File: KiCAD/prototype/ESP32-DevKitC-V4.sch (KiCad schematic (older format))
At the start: 27 parts

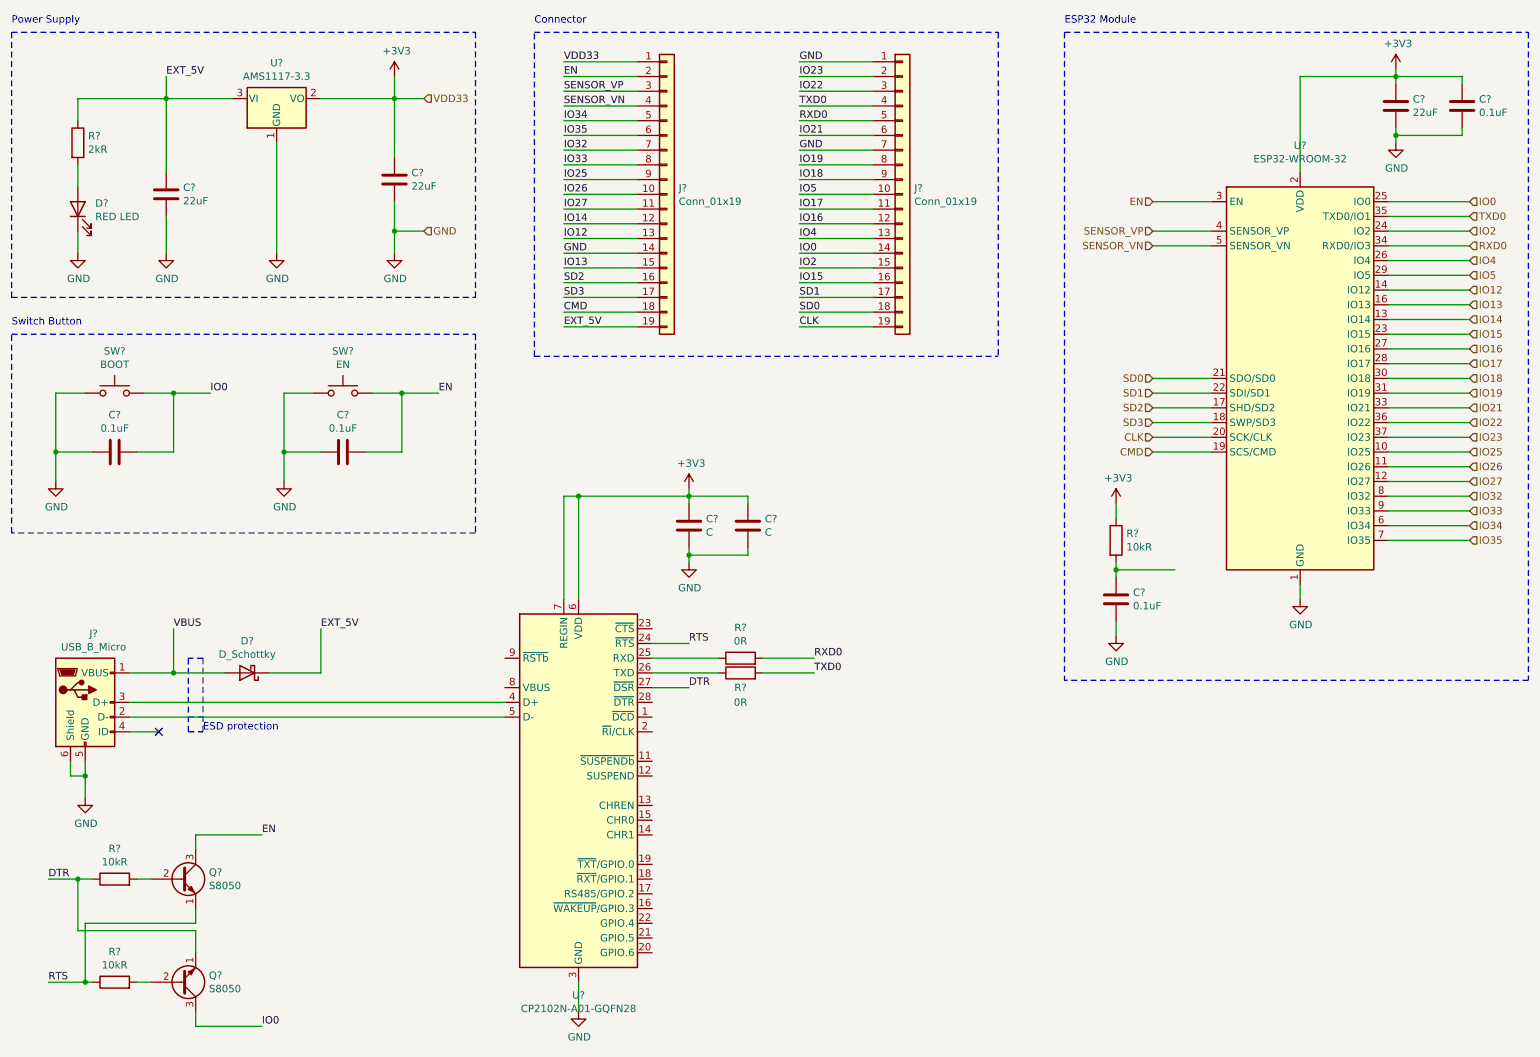
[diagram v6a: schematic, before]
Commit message: Add missing connections on ESP32-DevKitC-V4
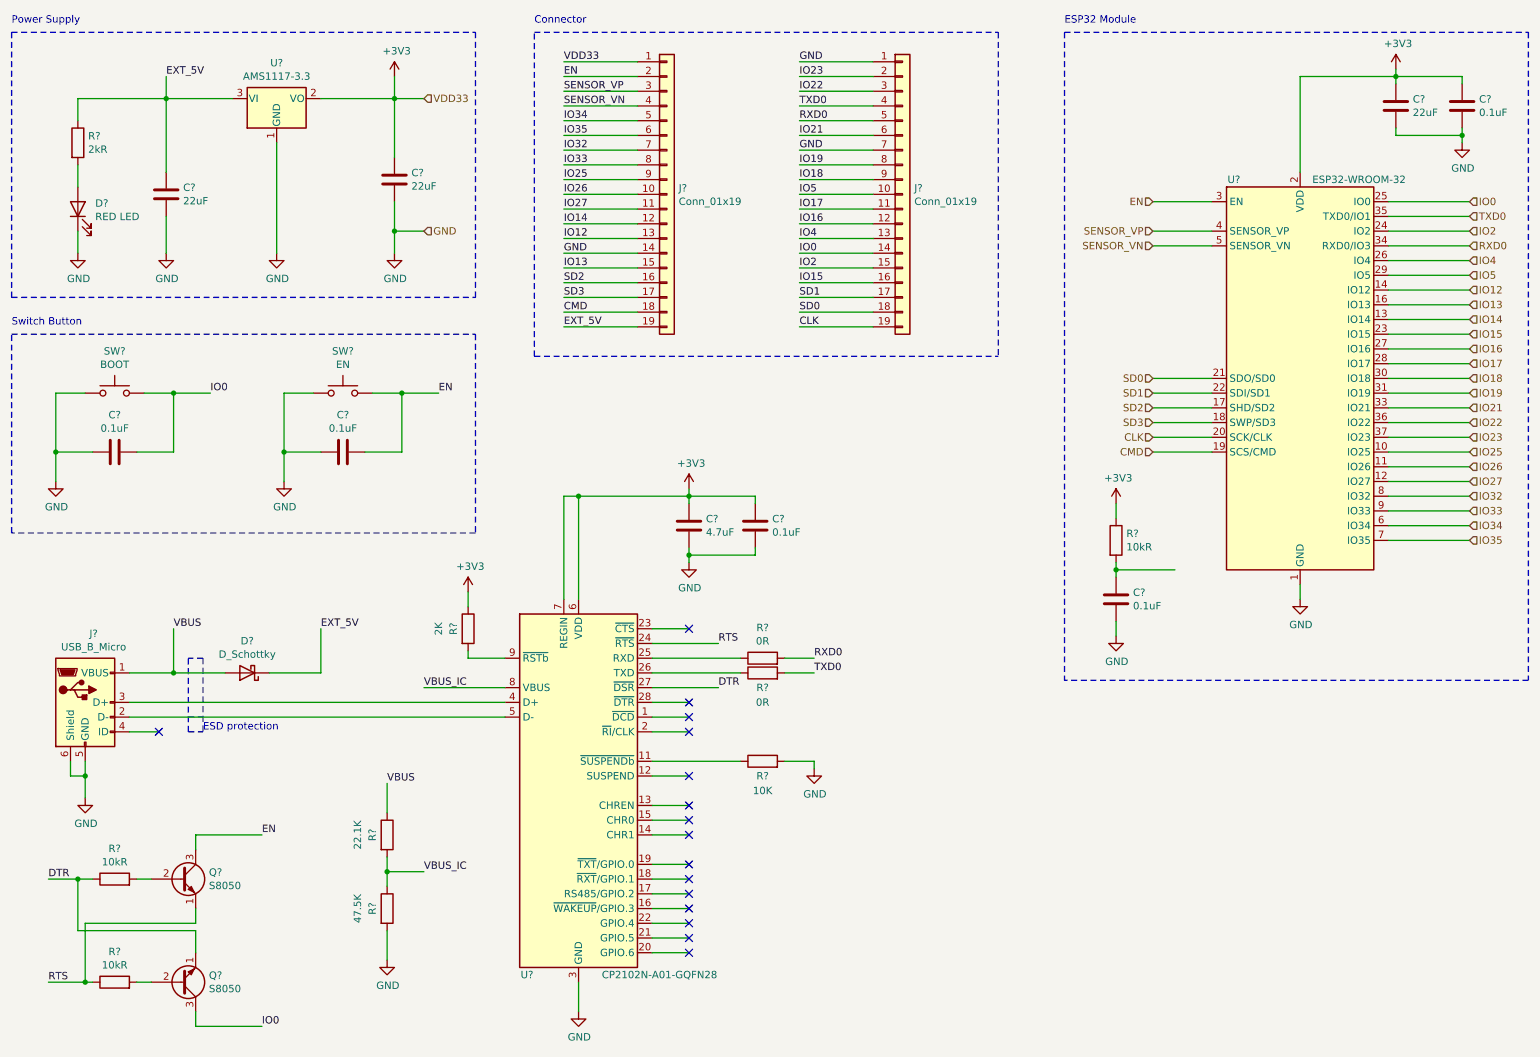
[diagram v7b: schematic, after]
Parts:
- added R?: 10K, symbol Device:R
- added R?: 2K, symbol Device:R
- added R?: 22.1K, symbol Device:R
- added R?: 47.5K, symbol Device:R
- C?: value C -> 4.7uF
- C?: value C -> 0.1uF
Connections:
- net +3V3: now also R?.1
- net GND: now also R?.2, R?.2
- net VBUS: now also R?.1
- net at U?.11 (~SUSPENDb): now also R?.1
- net VBUS_IC: now reaches U?.8 (VBUS)
- net VBUS_IC: now also R?.1, R?.2
- net at U?.9 (~RSTb): now also R?.2
- no-connect marks 1 -> 16
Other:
- moved on the sheet: C?, R?
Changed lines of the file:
@@
 U 1 1 5F93B762
 P 9450 3050
-F 0 "U?" H 9450 4631 50  0000 C CNN
-F 1 "ESP32-WROOM-32" H 9450 4540 50  0000 C CNN
+F 0 "U?" H 9000 4400 50  0000 C CNN
+F 1 "ESP32-WROOM-32" H 9850 4400 50  0000 C CNN
 F 2 "RF_Module:ESP32-WROOM-32" H 9450 1550 50  0001 C CNN
 F 3 "https://www.espressif.com/sites/default/files/documentation/esp32-wroom-32_datasheet_en.pdf" H 9150 3100 50  0001 C CNN
@@
 L power:GND #PWR?
 U 1 1 5F947B11
-P 10100 1450
-F 0 "#PWR?" H 10100 1200 50  0001 C CNN
-F 1 "GND" H 10105 1277 50  0000 C CNN
-F 2 "" H 10100 1450 50  0001 C CNN
-F 3 "" H 10100 1450 50  0001 C CNN
-	1    10100 1450
-	1    0    0    -1
-$EndComp
-Wire Wire Line
-	10100 1450 10100 1400
-Connection ~ 10100 1400
+P 10550 1450
+F 0 "#PWR?" H 10550 1200 50  0001 C CNN
+F 1 "GND" H 10555 1277 50  0000 C CNN
+F 2 "" H 10550 1450 50  0001 C CNN
+F 3 "" H 10550 1450 50  0001 C CNN
+	1    10550 1450
+	1    0    0    -1
+$EndComp
 Wire Wire Line
 	9450 1650 9450 1000
@@
 U 1 1 5FAB1912
 P 4550 5850
-F 0 "U?" H 4550 4461 50  0000 C CNN
-F 1 "CP2102N-A01-GQFN28" H 4550 4370 50  0000 C CNN
+F 0 "U?" H 4200 4600 50  0000 C CNN
+F 1 "CP2102N-A01-GQFN28" H 5100 4600 50  0000 C CNN
 F 2 "Package_DFN_QFN:QFN-28-1EP_5x5mm_P0.5mm_EP3.35x3.35mm" H 5000 4650 50  0001 L CNN
 F 3 "https://www.silabs.com/documents/public/data-sheets/cp2102n-datasheet.pdf" H 4600 5100 50  0001 C CNN
@@
 Wire Wire Line
 	1800 5050 2150 5050
-Wire Wire Line
-	5050 4950 5500 4950
-Wire Wire Line
-	5050 5050 5500 5050
 $Comp
 L Device:R R?
 U 1 1 5FB2E911
-P 5650 4950
-F 0 "R?" V 5857 4950 50  0000 C CNN
-F 1 "0R" V 5766 4950 50  0000 C CNN
-F 2 "" V 5580 4950 50  0001 C CNN
-F 3 "~" H 5650 4950 50  0001 C CNN
-	1    5650 4950
+P 5800 4950
+F 0 "R?" V 6007 4950 50  0000 C CNN
+F 1 "0R" V 5916 4950 50  0000 C CNN
+F 2 "" V 5730 4950 50  0001 C CNN
+F 3 "~" H 5800 4950 50  0001 C CNN
+	1    5800 4950
 	0    -1   -1   0
 $EndComp
@@
 L Device:R R?
 U 1 1 5FB2EF52
-P 5650 5050
-F 0 "R?" V 5550 5050 50  0000 C CNN
-F 1 "0R" V 5450 5050 50  0000 C CNN
-F 2 "" V 5580 5050 50  0001 C CNN
-F 3 "~" H 5650 5050 50  0001 C CNN
-	1    5650 5050
+P 5800 5050
+F 0 "R?" V 5700 5050 50  0000 C CNN
+F 1 "0R" V 5600 5050 50  0000 C CNN
+F 2 "" V 5730 5050 50  0001 C CNN
+F 3 "~" H 5800 5050 50  0001 C CNN
+	1    5800 5050
 	0    -1   -1   0
 $EndComp
-Wire Wire Line
-	5800 4950 6150 4950
-Wire Wire Line
-	5800 5050 6150 5050
 Text Label 6150 4950 0    50   ~ 0
 RXD0
 Text Label 6150 5050 0    50   ~ 0
 TXD0
-Wire Wire Line
-	5050 4850 5300 4850
-Wire Wire Line
-	5050 5150 5300 5150
-Text Label 5300 4850 0    50   ~ 0
+Text Label 5500 4850 0    50   ~ 0
 RTS
-Text Label 5300 5150 0    50   ~ 0
+Text Label 5500 5150 0    50   ~ 0
 DTR
 $Comp
@@
 P 5300 4050
 F 0 "C?" H 5415 4096 50  0000 L CNN
-F 1 "C" H 5415 4005 50  0000 L CNN
+F 1 "4.7uF" H 5415 4005 50  0000 L CNN
 F 2 "" H 5338 3900 50  0001 C CNN
 F 3 "~" H 5300 4050 50  0001 C CNN
@@
 L Device:C C?
 U 1 1 5FC16F78
-P 5700 4050
-F 0 "C?" H 5815 4096 50  0000 L CNN
-F 1 "C" H 5815 4005 50  0000 L CNN
-F 2 "" H 5738 3900 50  0001 C CNN
-F 3 "~" H 5700 4050 50  0001 C CNN
-	1    5700 4050
+P 5750 4050
+F 0 "C?" H 5865 4096 50  0000 L CNN
+F 1 "0.1uF" H 5865 4005 50  0000 L CNN
+F 2 "" H 5788 3900 50  0001 C CNN
+F 3 "~" H 5750 4050 50  0001 C CNN
+	1    5750 4050
 	1    0    0    -1
 $EndComp
 Wire Wire Line
 	5300 3800 5300 3850
-Wire Wire Line
-	5700 3900 5700 3850
-Wire Wire Line
-	5700 3850 5300 3850
 Connection ~ 5300 3850
 Wire Wire Line
@@
 Wire Wire Line
 	5300 4200 5300 4250
-Wire Wire Line
-	5700 4200 5700 4250
-Wire Wire Line
-	5700 4250 5300 4250
 Connection ~ 5300 4250
 Wire Wire Line
@@
 Text HLabel 3500 2050 2    50   Input ~ 0
 GND
+$Comp
+L Device:R R?
+U 1 1 5FBA030C
+P 5800 5650
+F 0 "R?" V 5700 5650 50  0000 C CNN
+F 1 "10K" V 5600 5650 50  0000 C CNN
+F 2 "" V 5730 5650 50  0001 C CNN
+F 3 "~" H 5800 5650 50  0001 C CNN
+	1    5800 5650
+	0    -1   -1   0
+$EndComp
+$Comp
+L power:GND #PWR?
+U 1 1 5FBA9E06
+P 6150 5700
+F 0 "#PWR?" H 6150 5450 50  0001 C CNN
+F 1 "GND" H 6155 5527 50  0000 C CNN
+F 2 "" H 6150 5700 50  0001 C CNN
+F 3 "" H 6150 5700 50  0001 C CNN
+	1    6150 5700
+	1    0    0    -1
+$EndComp
+Wire Wire Line
+	5050 5750 5300 5750
+NoConn ~ 5300 5750
+$Comp
+L Device:R R?
+U 1 1 5FBC736A
+P 3800 4750
+F 0 "R?" V 3700 4750 50  0000 C CNN
+F 1 "2K" V 3600 4750 50  0000 C CNN
+F 2 "" V 3730 4750 50  0001 C CNN
+F 3 "~" H 3800 4750 50  0001 C CNN
+	1    3800 4750
+	1    0    0    -1
+$EndComp
+Wire Wire Line
+	3800 4950 4050 4950
+$Comp
+L power:+3V3 #PWR?
+U 1 1 5FBD18A0
+P 3800 4500
+F 0 "#PWR?" H 3800 4350 50  0001 C CNN
+F 1 "+3V3" H 3815 4673 50  0000 C CNN
+F 2 "" H 3800 4500 50  0001 C CNN
+F 3 "" H 3800 4500 50  0001 C CNN
+	1    3800 4500
+	1    0    0    -1
+$EndComp
+Wire Wire Line
+	3800 4950 3800 4900
+Wire Wire Line
+	3800 4500 3800 4600
+Text Label 3500 5150 0    50   ~ 0
+VBUS_IC
+Wire Wire Line
+	3500 5150 4050 5150
+Text Label 3250 5800 0    50   ~ 0
+VBUS
+Wire Wire Line
+	3250 5800 3250 6000
+$Comp
+L Device:R R?
+U 1 1 5FC24EFD
+P 3250 6150
+F 0 "R?" V 3150 6150 50  0000 C CNN
+F 1 "22.1K" V 3050 6150 50  0000 C CNN
+F 2 "" V 3180 6150 50  0001 C CNN
+F 3 "~" H 3250 6150 50  0001 C CNN
+	1    3250 6150
+	1    0    0    -1
+$EndComp
+$Comp
+L Device:R R?
+U 1 1 5FC254AB
+P 3250 6650
+F 0 "R?" V 3150 6650 50  0000 C CNN
+F 1 "47.5K" V 3050 6650 50  0000 C CNN
+F 2 "" V 3180 6650 50  0001 C CNN
+F 3 "~" H 3250 6650 50  0001 C CNN
+	1    3250 6650
+	1    0    0    -1
+$EndComp
+$Comp
+L power:GND #PWR?
+U 1 1 5FC259A6
+P 3250 7000
+F 0 "#PWR?" H 3250 6750 50  0001 C CNN
+F 1 "GND" H 3255 6827 50  0000 C CNN
+F 2 "" H 3250 7000 50  0001 C CNN
+F 3 "" H 3250 7000 50  0001 C CNN
+	1    3250 7000
+	1    0    0    -1
+$EndComp
+Wire Wire Line
+	3250 7000 3250 6800
+Wire Wire Line
+	3250 6500 3250 6400
+Wire Wire Line
+	3250 6400 3500 6400
+Connection ~ 3250 6400
+Wire Wire Line
+	3250 6400 3250 6300
+Text Label 3500 6400 0    50   ~ 0
+VBUS_IC
+Wire Wire Line
+	5750 3850 5750 3900
+Wire Wire Line
+	5300 3850 5750 3850
+Wire Wire Line
+	5750 4250 5750 4200
+Wire Wire Line
+	5300 4250 5750 4250
+Wire Wire Line
+	10550 1450 10550 1400
+Connection ~ 10550 1400
+Wire Wire Line
+	5050 5950 5300 5950
+Wire Wire Line
+	5050 6050 5300 6050
+Wire Wire Line
+	5050 6150 5300 6150
+Wire Wire Line
+	5050 6350 5300 6350
+Wire Wire Line
+	5050 6450 5300 6450
+Wire Wire Line
+	5050 6550 5300 6550
+Wire Wire Line
+	5050 6650 5300 6650
+Wire Wire Line
+	5050 6750 5300 6750
+Wire Wire Line
+	5050 6850 5300 6850
+Wire Wire Line
+	5050 6950 5300 6950
+NoConn ~ 5300 6050
+NoConn ~ 5300 6650
+NoConn ~ 5300 6550
+NoConn ~ 5300 6450
+NoConn ~ 5300 6350
+NoConn ~ 5300 6950
+NoConn ~ 5300 6850
+NoConn ~ 5300 6750
+NoConn ~ 5300 5950
+NoConn ~ 5300 6150
+Wire Wire Line
+	5050 5350 5300 5350
+Wire Wire Line
+	5050 5450 5300 5450
+NoConn ~ 5300 5450
+NoConn ~ 5300 5350
+Wire Wire Line
+	5050 4750 5300 4750
+Wire Wire Line
+	5050 5250 5300 5250
+NoConn ~ 5300 5250
+NoConn ~ 5300 4750
+Wire Wire Line
+	5950 4950 6150 4950
+Wire Wire Line
+	5950 5050 6150 5050
+Wire Wire Line
+	5050 4950 5650 4950
+Wire Wire Line
+	5050 5050 5650 5050
+Wire Wire Line
+	5050 5650 5650 5650
+Wire Wire Line
+	6150 5650 6150 5700
+Wire Wire Line
+	5950 5650 6150 5650
+Wire Wire Line
+	5050 5150 5500 5150
+Wire Wire Line
+	5050 4850 5500 4850
 $EndSCHEMATC

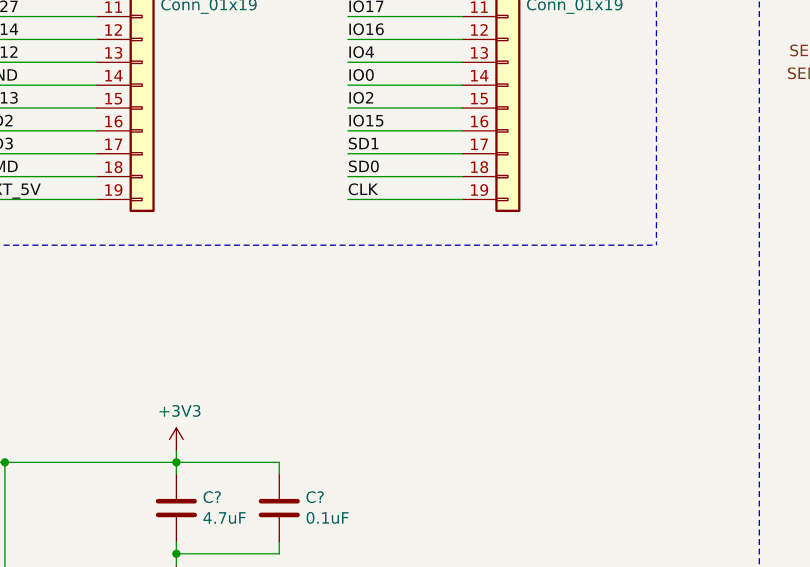
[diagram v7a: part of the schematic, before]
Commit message: Adicionadas as ligações entre componentes
Necessário verificar quais sheets não estão a ser utilizadas e eliminar
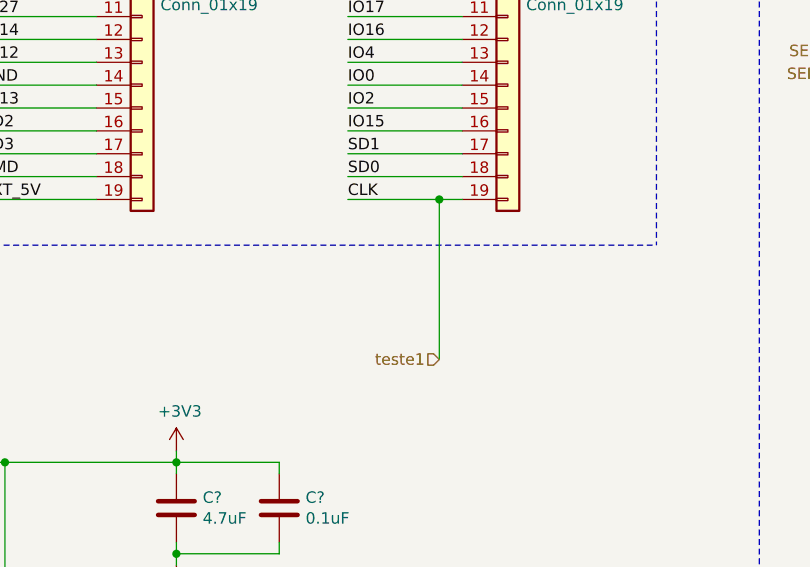
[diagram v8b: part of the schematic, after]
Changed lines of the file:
@@
 $Descr A4 11693 8268
 encoding utf-8
-Sheet 2 2
+Sheet 2 6
 Title "ESP32-DevKitC-V4"
 Date "2020-10-23"
@@
 	6550 2600 6050 2600
 Wire Wire Line
-	6550 2700 6050 2700
+	6550 2700 6450 2700
 Text Label 6050 900  0    50   ~ 0
 GND
@@
 Wire Wire Line
 	5050 4850 5500 4850
+Text HLabel 6450 3400 0    50   Input ~ 0
+teste1
+Wire Wire Line
+	6450 3400 6450 2700
+Connection ~ 6450 2700
+Wire Wire Line
+	6450 2700 6050 2700
 $EndSCHEMATC
